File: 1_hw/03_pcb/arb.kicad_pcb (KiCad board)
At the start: 4 copper layers, 100 x 100 mm, 268 parts, among them J1 TYPE-C-31-M-12, J2 SMA, J3 SMA, J4 BNC, J5 PH-00244, SW1 TS-1187A-B-A-B, SW2 SS-12D02-VG4, SW3 SS-12D02-VG4, U1 TLV70333DBV, U10 LMK1C1103PWR, U11 STM32F446ZETx, U12 ICE40UP5K-SG48ITR, U13 93LC56BT-I_OT, U14 FT2232HL, U15 W25Q128JVSIQ, U16 W25Q128JVSIQ, U17 AD9850, U18 AD9744, U19 LM6171, U2 TLV76133DCY, U20 LM6171, U21 TMUX6104, U22 TPL0401B-10, U23 THS3491, U24 ADG1219BRJZ, U25 LM6171, U26 TMUX6104, U3 TLV70333DBV, U4 LM3880MF-1AA, U5 TLV70312DBV, U6 TLV70325DBV, U7 TPS65131RGE, U8 TPD2E001DRL, U9 ADG1219BRJZ, X1 ASE-10.000MHz, X2 ASE-100.000MHz, Y1 32.768k, Y2 12 MHz

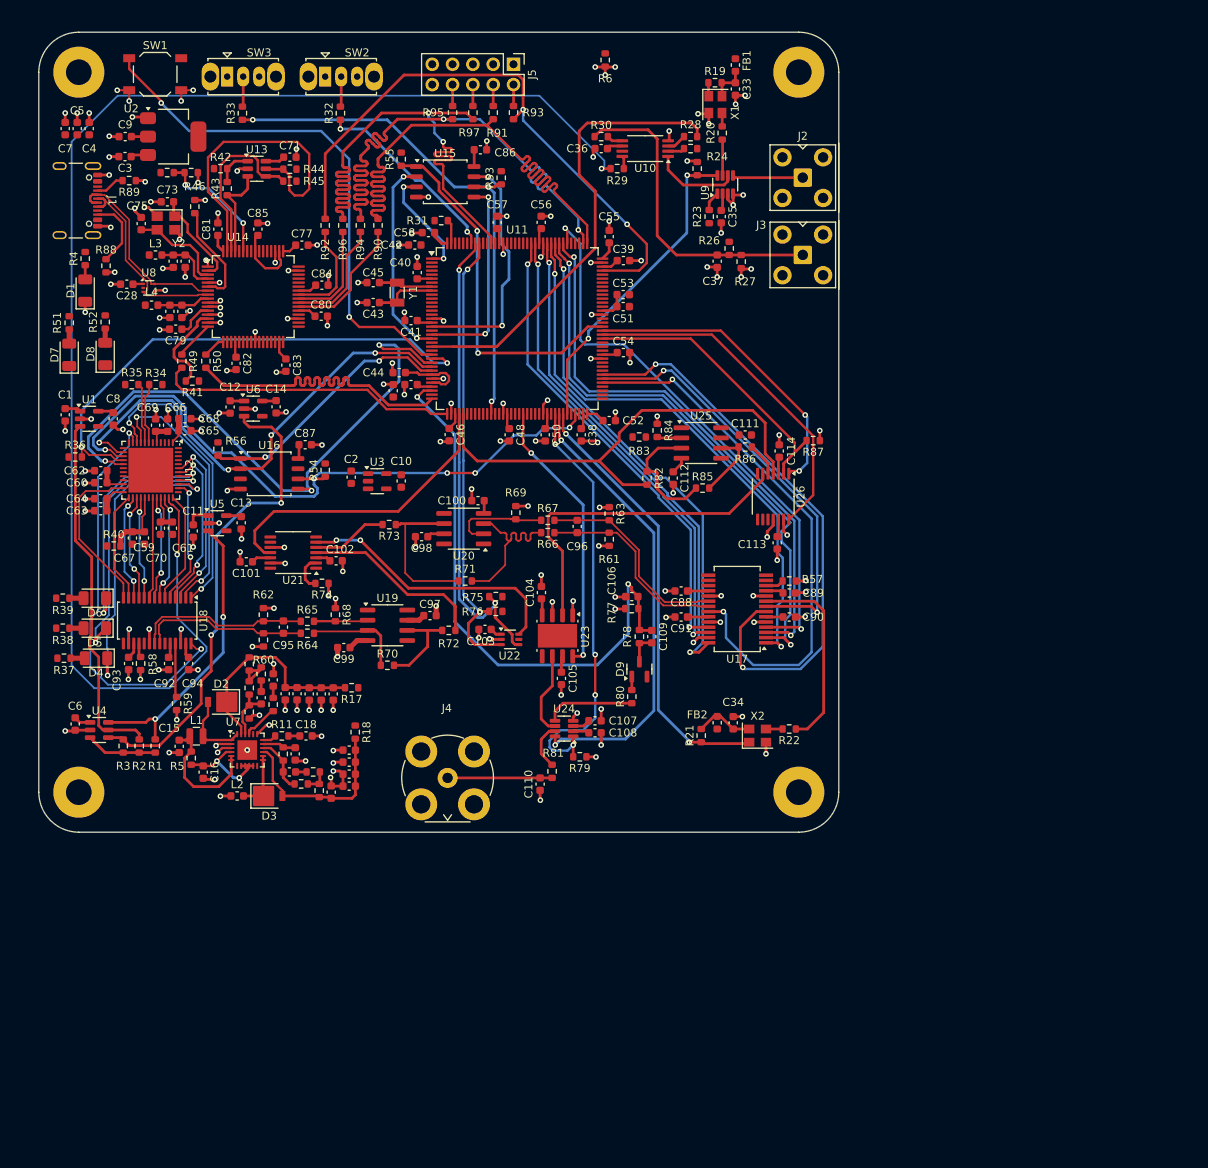
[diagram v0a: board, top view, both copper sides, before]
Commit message: MINOR: Removed all existing Vias and Tracks.
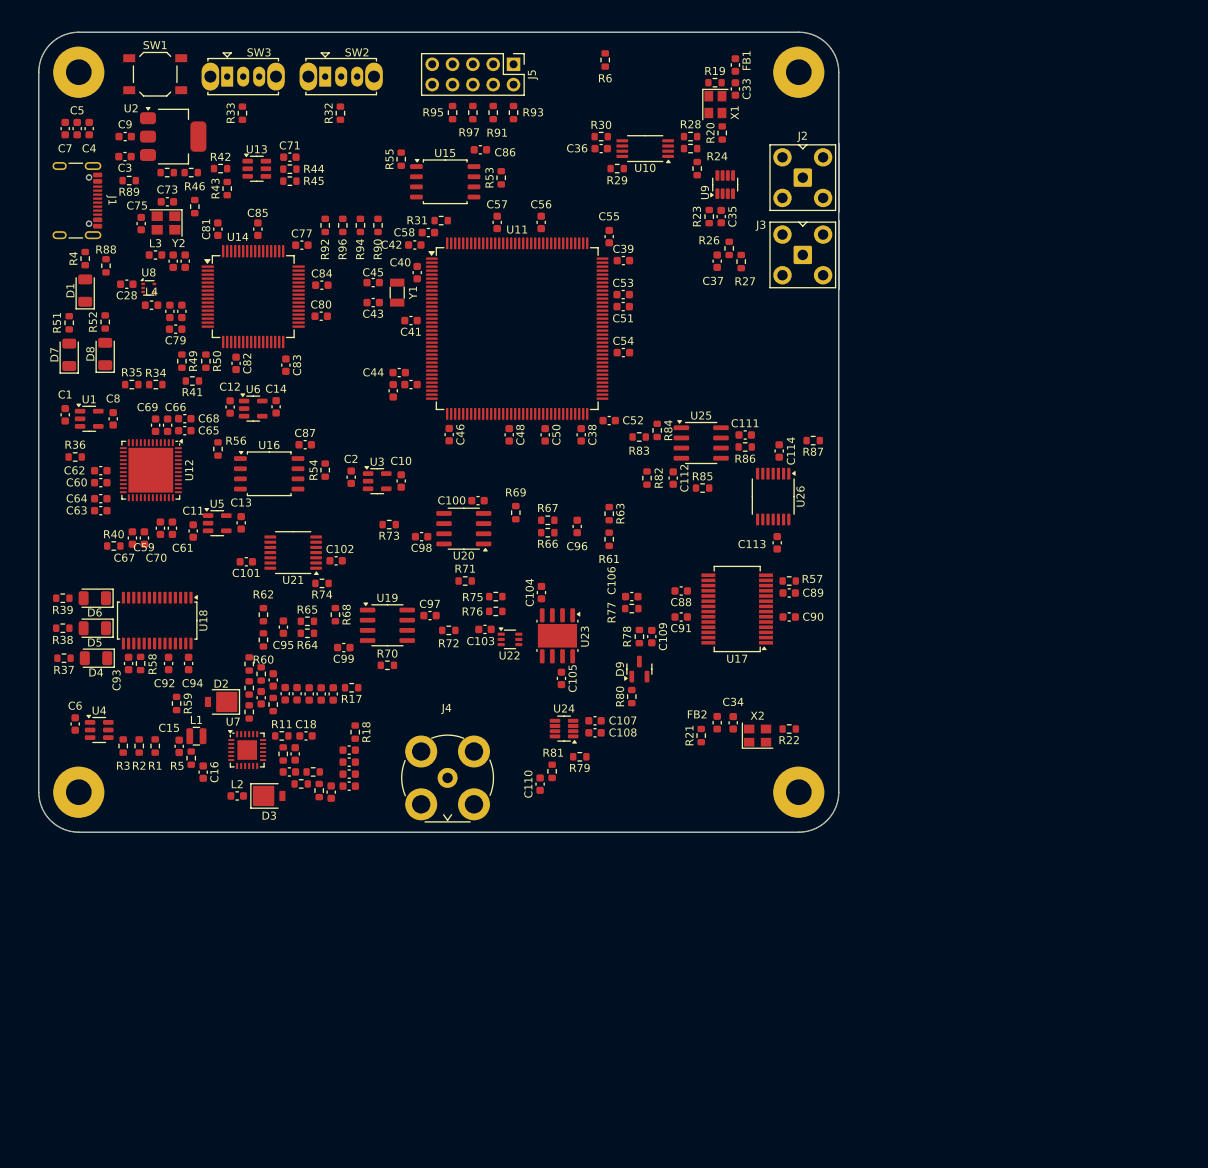
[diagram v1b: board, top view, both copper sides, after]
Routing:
- net GND: track 261.4 -> 0.00 mm, vias 189 -> 0
- net CLK_10MHZ_DIST_FPGA_3P3: track 181.4 -> 0.00 mm, vias 2 -> 0
- net SPI_SCLK_MCU_FPGA_3P3: track 84.1 -> 0.00 mm, vias 5 -> 0
- net 3P3V_D: track 78.7 -> 0.00 mm
- net ANALOG_DC-OFFSET_AMUX3_AMP3: track 76.8 -> 0.00 mm, vias 2 -> 0
- net SPI_MOSI_MCU_FPGA_3P3: track 76.6 -> 0.00 mm, vias 3 -> 0
- net JTAG_MCU_TMS_3P3: track 74.1 -> 0.00 mm, vias 2 -> 0
- net GPIO_D2_MCU_DDS_3P3: track 72.7 -> 0.00 mm, vias 2 -> 0
- net GPIO_W-CLK_MCU_DDS_3P3: track 72.6 -> 0.00 mm, vias 2 -> 0
- net ANALOG_CAL-ADC_AMUX2_MCU: track 71.9 -> 0.00 mm, vias 2 -> 0
- net GPIO_D0_MCU_DDS_3P3: track 71.7 -> 0.00 mm, vias 2 -> 0
- net JTAG_MCU_TDI_3P3: track 71.6 -> 0.00 mm, vias 2 -> 0
- net JTAG_MCU_TCK_3P3: track 71.0 -> 0.00 mm
- net GPIO_D3_MCU_DDS_3P3: track 70.4 -> 0.00 mm, vias 2 -> 0
- net GPIO_D1_MCU_DDS_3P3: track 70.2 -> 0.00 mm, vias 2 -> 0
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
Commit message: FEAT: Placed components for Left-Handed Analog Output.
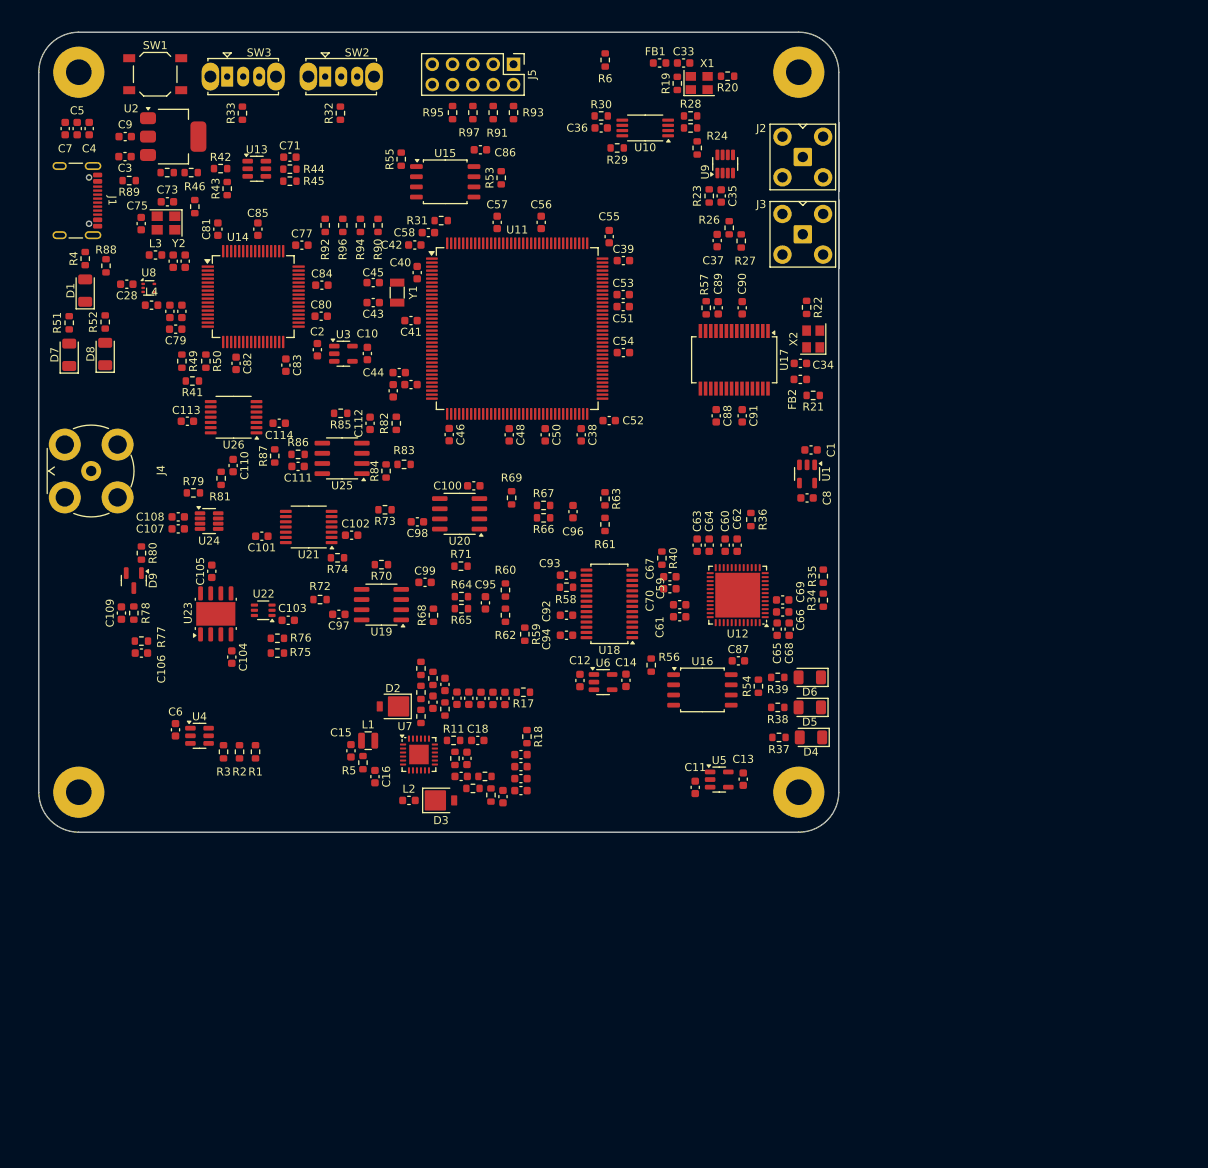
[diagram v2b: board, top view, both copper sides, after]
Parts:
- moved C1 93.3 mm to (197.2, 95.2), turned to 180 degrees
- moved U1 90.0 mm to (196.7, 98.2), turned to -90 degrees
- moved D4 89.9 mm to (197.2, 131.1)
- moved R37 89.9 mm to (193.2, 131.1)
- moved D5 89.9 mm to (197.1, 127.3)
- moved D6 89.9 mm to (197.1, 123.6)
- moved R38 89.9 mm to (193.1, 127.3)
- moved R39 89.9 mm to (193.1, 123.6)
- moved R35 89.7 mm to (198.8, 110.9), turned to 90 degrees
- moved R34 87.7 mm to (198.8, 113.9), turned to -90 degrees
- moved C8 87.3 mm to (196.7, 101.2), turned to 180 degrees
- moved R36 84.8 mm to (189.7, 103.9), turned to 90 degrees
- moved C69 81.4 mm to (193.7, 113.9), turned to 0 degrees
- moved C66 80.4 mm to (193.7, 115.4), turned to 0 degrees
- moved C62 80.1 mm to (188.0, 107.1), turned to 90 degrees
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
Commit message: FEAT: Placed most components for Right-Handed Analog Output.
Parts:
- moved D4 98.0 mm to (112.3, 180.0)
- moved R37 98.0 mm to (108.3, 180.0)
- moved D5 98.0 mm to (112.2, 176.2)
- moved D6 98.0 mm to (112.2, 172.5)
- moved R38 98.0 mm to (108.2, 176.2)
- moved R39 98.0 mm to (108.2, 172.5)
- moved J4 91.2 mm to (195.2, 121.9), turned to -90 degrees
- moved R34 90.0 mm to (111.7, 136.7), turned to 180 degrees
- moved R35 87.9 mm to (114.7, 136.7), turned to 0 degrees
- moved C68 87.7 mm to (108.1, 132.5), turned to 180 degrees
- moved C65 85.9 mm to (108.1, 131.0), turned to 180 degrees
- moved C66 85.0 mm to (110.3, 131.7), turned to -90 degrees
- moved C69 83.8 mm to (111.8, 131.7), turned to -90 degrees
- moved U12 76.8 mm to (112.4, 126.0), turned to 90 degrees
- moved R36 72.0 mm to (121.8, 127.7), turned to 0 degrees
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
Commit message: FEAT: Added some Power Planes for 3.3V, 5V. Routed 50 Ohm Analog and Differential.
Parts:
- moved C1 123.4 mm to (118.3, 133.2), turned to -90 degrees
- moved U1 120.2 mm to (121.3, 133.7), turned to 0 degrees
- moved C8 117.6 mm to (124.3, 133.7), turned to -90 degrees
- moved R37 92.0 mm to (103.1, 88.2), turned to -90 degrees
- moved D4 88.3 mm to (103.1, 92.2), turned to 90 degrees
- moved R38 88.2 mm to (106.8, 88.0), turned to -90 degrees
- moved R39 84.5 mm to (110.6, 88.0), turned to -90 degrees
- moved D5 84.4 mm to (106.8, 92.0), turned to 90 degrees
- moved D6 80.5 mm to (110.6, 92.0), turned to 90 degrees
- moved C12 70.1 mm to (128.0, 133.8)
- moved C14 70.1 mm to (133.7, 133.8)
- moved U6 70.1 mm to (130.9, 134.0)
- moved R54 51.3 mm to (134.3, 119.7)
- moved U16 51.3 mm to (127.3, 120.2)
- moved C87 51.3 mm to (131.8, 116.5)
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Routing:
- net ANALOG_DC-OFFSET_AMUX3_AMP3: track 0.00 -> 45.5 mm
- net ANALOG_DAC2_MCU_AMUX3: track 0.00 -> 34.7 mm
- net ANALOG_DDS_OUT_P: track 0.00 -> 23.7 mm
- net ANALOG_DDS_OUT_N: track 0.00 -> 21.4 mm
- net Net-(U20-+): track 0.00 -> 20.7 mm
- net Net-(R71-Pad2): track 0.00 -> 19.7 mm
- net Net-(U19-+): track 0.00 -> 18.1 mm
- net Net-(U22-W): track 0.00 -> 16.3 mm
- net ANALOG_FPGA-DAC_OUT_N: track 0.00 -> 15.7 mm
- net ANALOG_FPGA-DAC_OUT_P: track 0.00 -> 15.3 mm
- net Net-(R70-Pad2): track 0.00 -> 13.2 mm
- net ANALOG_STAGE-2_AMUX2_EXT: track 0.00 -> 11.7 mm
- net Net-(U26-S2): track 0.00 -> 11.6 mm, vias 0 -> 2
- net Net-(U20--): track 0.00 -> 11.4 mm
- net Net-(U24-SB): track 0.00 -> 10.5 mm
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- added copper zone on B.Cu, net 3P3V_D
- added copper zone on B.Cu, net 5P0V

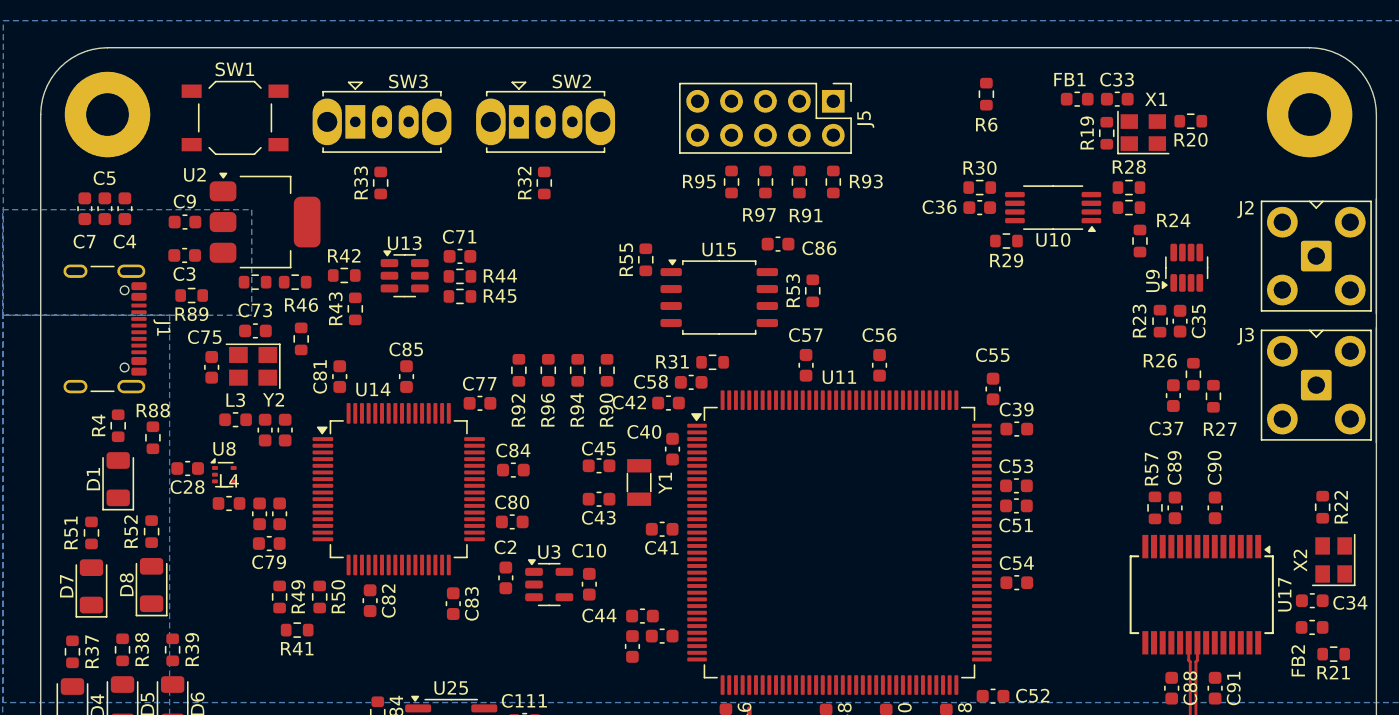
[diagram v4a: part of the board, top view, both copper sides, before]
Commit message: MINOR: Continuing layout. USB, Some FTDI, etc.
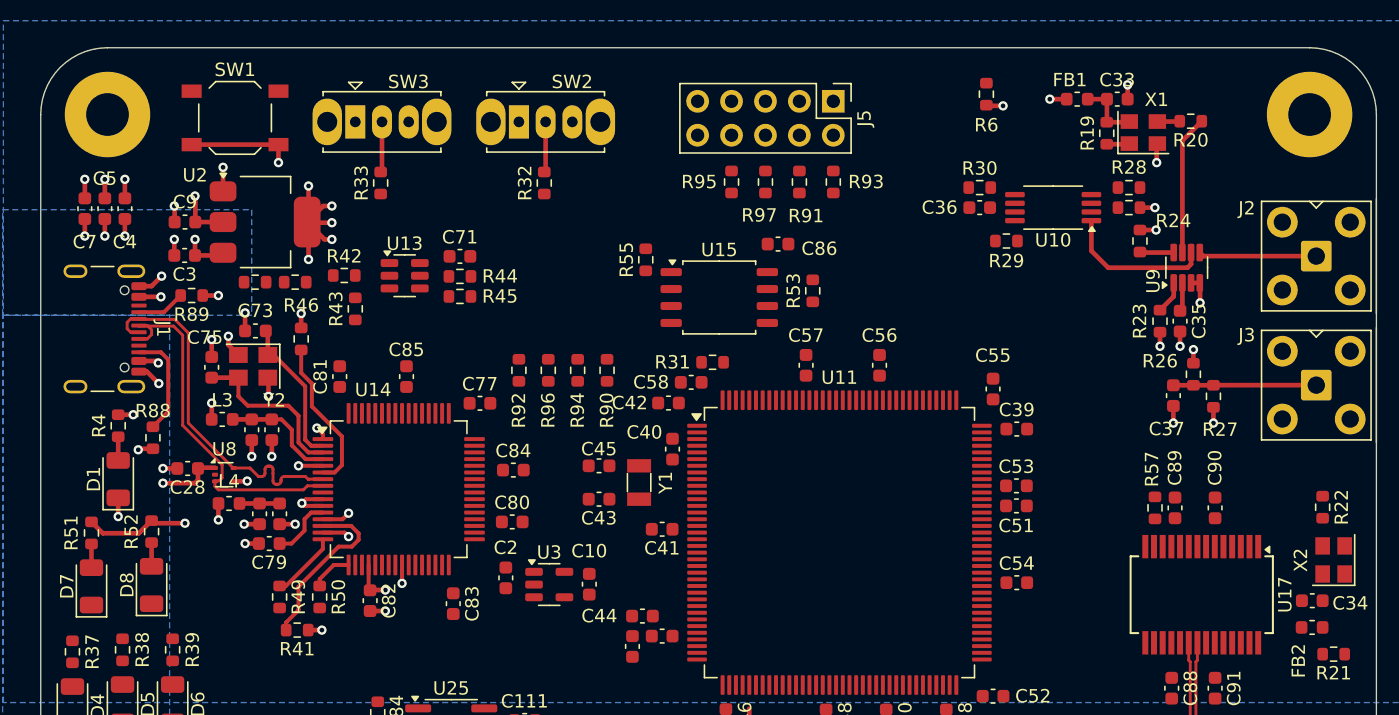
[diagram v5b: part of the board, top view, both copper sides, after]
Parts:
- moved C72 1.00 mm to (116.5, 71.5)
- moved C76 1.00 mm to (118.0, 71.5)
- moved L3 1.00 mm to (114.3, 70.8)
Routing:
- net GND: track 2.50 -> 64.7 mm, vias 2 -> 41
- net 3P3V_D: track 0.00 -> 37.2 mm, vias 0 -> 15
- net USB_DATA_CONN_FTDI_P: track 0.00 -> 27.4 mm
- net USB_DATA_CONN_FTDI_N: track 0.00 -> 27.2 mm
- net 5P0V: track 0.00 -> 16.4 mm, vias 0 -> 8
- net Net-(U14-~{RESET}): track 0.00 -> 13.0 mm
- net Net-(U14-OSCO): track 0.00 -> 12.6 mm
- net Net-(U14-REF): track 0.00 -> 11.5 mm
- net Net-(U10-CLKIN): track 0.00 -> 11.2 mm
- net Net-(U14-OSCI): track 0.00 -> 11.1 mm
- net CLK_10MHZ_DIST_EXT_3P3: track 0.00 -> 10.7 mm
- net Net-(U9-SA): track 0.00 -> 10.4 mm
- net CLK_10MHZ_EXT_SW_3P3: track 0.00 -> 8.84 mm
- net Net-(U14-VPHY): track 0.00 -> 8.67 mm
- net Net-(J1-CC2): track 0.00 -> 7.92 mm
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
